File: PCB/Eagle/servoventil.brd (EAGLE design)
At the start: 160 x 100 mm, 0 parts

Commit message: Rozdělané schéma
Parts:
- added C1, C2: 100n 1206, rcl:C1206
- added D1: LOW BAT 1206, SparkFun-LED:LED-1206
- added D2: STTH4R02S DO214AB, diode:DO214AA
- added DIP: DIP-4X_DIP, #PaJa_prepinace:DIP-4X
- added F1: 3,5A 1206, adafruit:R1206
- added IO1: ATTINY1634 SO20W, bt_avr:SOIC20
- added IO2: MCP1825 SOT223, bt_regulator:SOT-223-3
- added IO3: DS3231MZ+, SamacSys_Parts:SOIC127P600X175-8N
- added J1: ICSP 2x5, SparkFun-Connectors:2X5-SHROUDED_LOCK
- added J2: SERIAL, #PaJa_konektory:S1G5_JUM
- added K1: ARK500/2, #PaJa_konektory:ARK500/2
- added R1, R8: 10k 1206, rcl:R1206
- added R10, R9: 4k7 1206, rcl:R1206
- added R2: 10k 1203, rcl:R1206
- added R3: 1k 1206, rcl:R1206
- added R4: 47k 1206, rcl:R1206
- added R5: 2k7 1206, rcl:R1206
- added R6: 3k3 1206, rcl:R1206
- added R7: 100R 1206, rcl:R1206
- added S1: 6x6mm SMD, SparkFun-Switches:TACTILE_SWITCH_SMD_6.2MM_TALL
- added T1: DMP2100U SOT23, bt_transistor:SOT-23
- added T2: IRF7416PBF SO8, SamacSys_Parts:SOIC127P600X175-8N
- added T3: FDV303N SOT23, bt_transistor:SOT-23
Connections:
- new net 3,3V_VCC: C2.1, IO2.3, IO3.2, R10.1, R9.1
- new net 6V: C1.1, IO2.1, R5.2, T1.3
- new net GND: C1.2, C2.2, D1.C, D2.A, DIP.1, DIP.2, DIP.3, DIP.4, IO1.10, IO3.5, J1.10, J1.4, J1.6, J1.8, J2.1, K1.1, R4.1, R6.1, S1.A2, T3.2
- new net HEATSINK: IO2.2, IO2.4
- new net LED_LOWBAT_PIN: R7.1
- new net LOW_BAT_PIN: R5.1, R6.2
- new net N$1: F1.2, K1.2
- new net N$10: IO3.3
- new net N$12: D1.A, R7.2
- new net N$2: D2.C, F1.1, R1.2, R2.2, T1.2, T2.1, T2.2, T2.3
- new net N$3: R3.2, R4.2, T3.1
- new net N$5: J1.7
- new net N$6: J1.9
- new net N$7: J1.1
- new net PWR_ON_PIN: R3.1
- new net PWR_RTC_ON: R1.1, S1.B2, T1.1, T3.3
- new net PWR_SERVO_ON_PIN: R2.1, T2.4
- new net PWR_SERVO_OUT: T2.5, T2.6, T2.7, T2.8
- new net RESET: IO1.14, J1.5, J2.5, R8.2
- new net RX_PIN: J2.4
- new net SCL_PIN: IO3.8, R9.2
- new net SDA_PIN: IO3.7, R10.2
- new net SW1_PIN: DIP.8
- new net SW2_PIN: DIP.7
- new net SW3_PIN: DIP.6
- new net SW4_PIN: DIP.5
- new net TX_PIN: J2.3
- new net VCC: IO1.11, J1.2, J2.2, R8.1

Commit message: Schema před kontrolou
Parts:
- removed IO3: DS3231MZ+, SamacSys_Parts:SOIC127P600X175-8N
- removed S1: 6x6mm SMD, SparkFun-Switches:TACTILE_SWITCH_SMD_6.2MM_TALL
- added BT1: CR2032, SparkFun-Batteries:BATTCOM_20MM_PTH
- added IO3A: DS3231MZ+ SO8, SamacSys_Parts:SOIC127P600X175-8N
- added IO3B: DS3231SN SO16W, adafruit:SO16W
- added SW1: SPST_TACT-EVQQ2, adafruit:EVQ-Q2
- moved R10 251.6 mm to (66.0, 78.7), turned to 270 degrees
- moved R9 244.2 mm to (62.2, 78.7), turned to 270 degrees
- moved C1 205.0 mm to (133.3, 86.4)
- moved C2 205.0 mm to (133.3, 81.3)
- moved R1 205.0 mm to (133.3, 76.2)
- moved R2 205.0 mm to (133.3, 71.1)
- moved R3 205.0 mm to (128.3, 38.1)
- moved R4 205.0 mm to (128.3, 31.8)
- moved R5 205.0 mm to (128.3, 25.4)
- moved R6 205.0 mm to (128.3, 19.1)
- moved R7 205.0 mm to (115.6, 12.7)
- moved R8 205.0 mm to (115.6, 6.35)
- moved K1 202.6 mm to (144.8, 31.8)
- moved DIP 202.5 mm to (80.0, 57.1)
- moved T2 195.2 mm to (114.3, 50.8)
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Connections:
- removed net N$10: IO3.3
- removed net N$5: J1.7
- removed net N$6: J1.9
- removed net N$7: J1.1
- removed net SCL_PIN: IO3.8, R9.2
- removed net SDA_PIN: IO3.7, R10.2
- new net 3V: BT1.1, IO3A.6, IO3B.14
- new net MISO: IO1.19, J1.9
- new net MOSI_SDA_PIN: IO1.20, IO3A.7, IO3B.15, J1.1, R10.2
- new net SCK_SCL_PIN: IO1.16, IO3A.8, IO3B.16, J1.7, R9.2
- new net SERVO_PIN: IO1.4
- net 3,3V_VCC: now also IO3A.2, IO3B.2; no longer IO3.2
- net GND: now also BT1.2, IO3A.5, IO3B.10, IO3B.11, IO3B.12, IO3B.13, IO3B.5, IO3B.6, IO3B.7, IO3B.8, IO3B.9, SW1.A, SW1.A'; no longer IO3.5, S1.A2
- net LED_LOWBAT_PIN: now also IO1.7
- net LOW_BAT_PIN: now also IO1.6
- net PWR_ON_PIN: now also IO1.5
- net PWR_RTC_ON: now also IO3A.3, IO3B.3, SW1.B, SW1.B'; no longer S1.B2
- net PWR_SERVO_ON_PIN: now also IO1.3
- net RX_PIN: now also IO1.2
- net SW1_PIN: now also IO1.8
- net SW2_PIN: now also IO1.9
- net SW3_PIN: now also IO1.12
- net SW4_PIN: now also IO1.13
- net TX_PIN: now also IO1.1

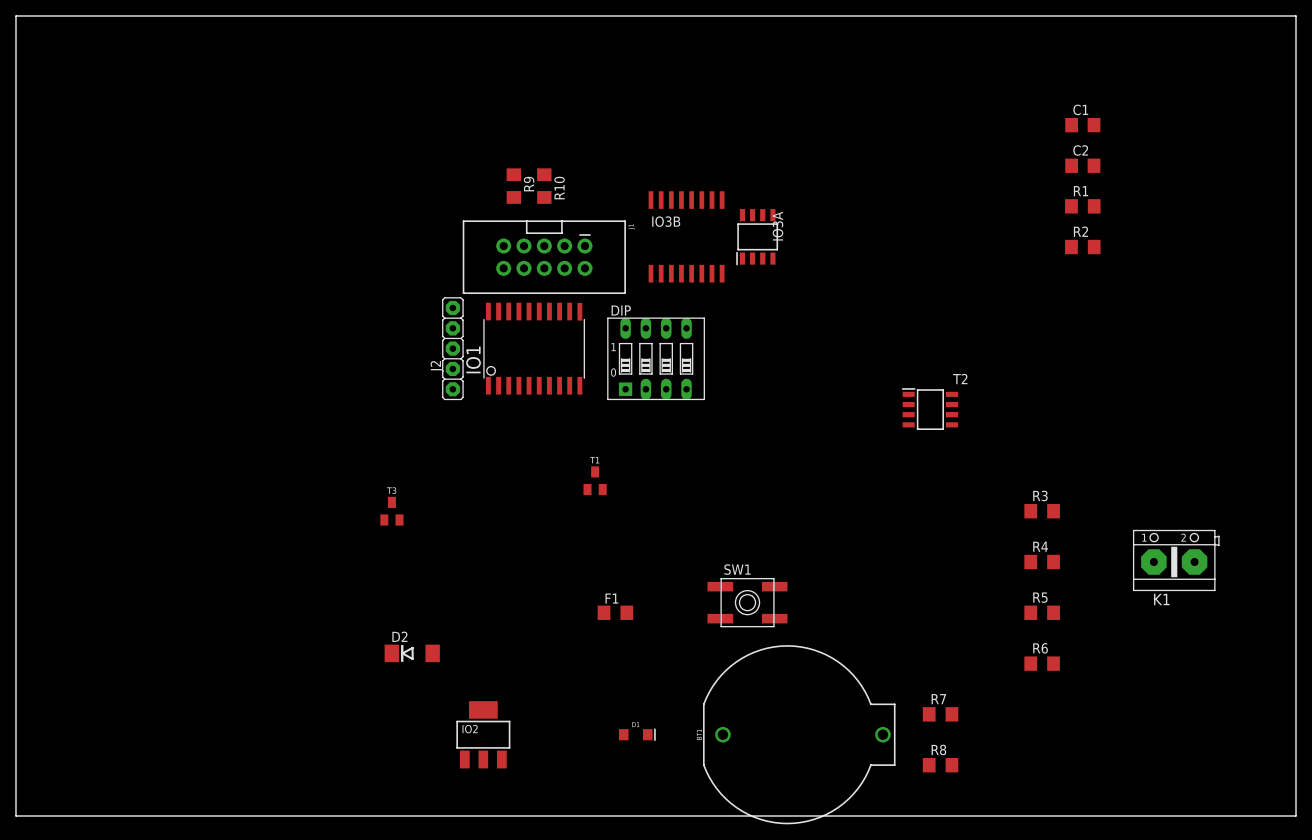
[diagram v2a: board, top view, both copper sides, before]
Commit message: Deska spojů, schéma
vše před kontrolou (až dorazí součástky)
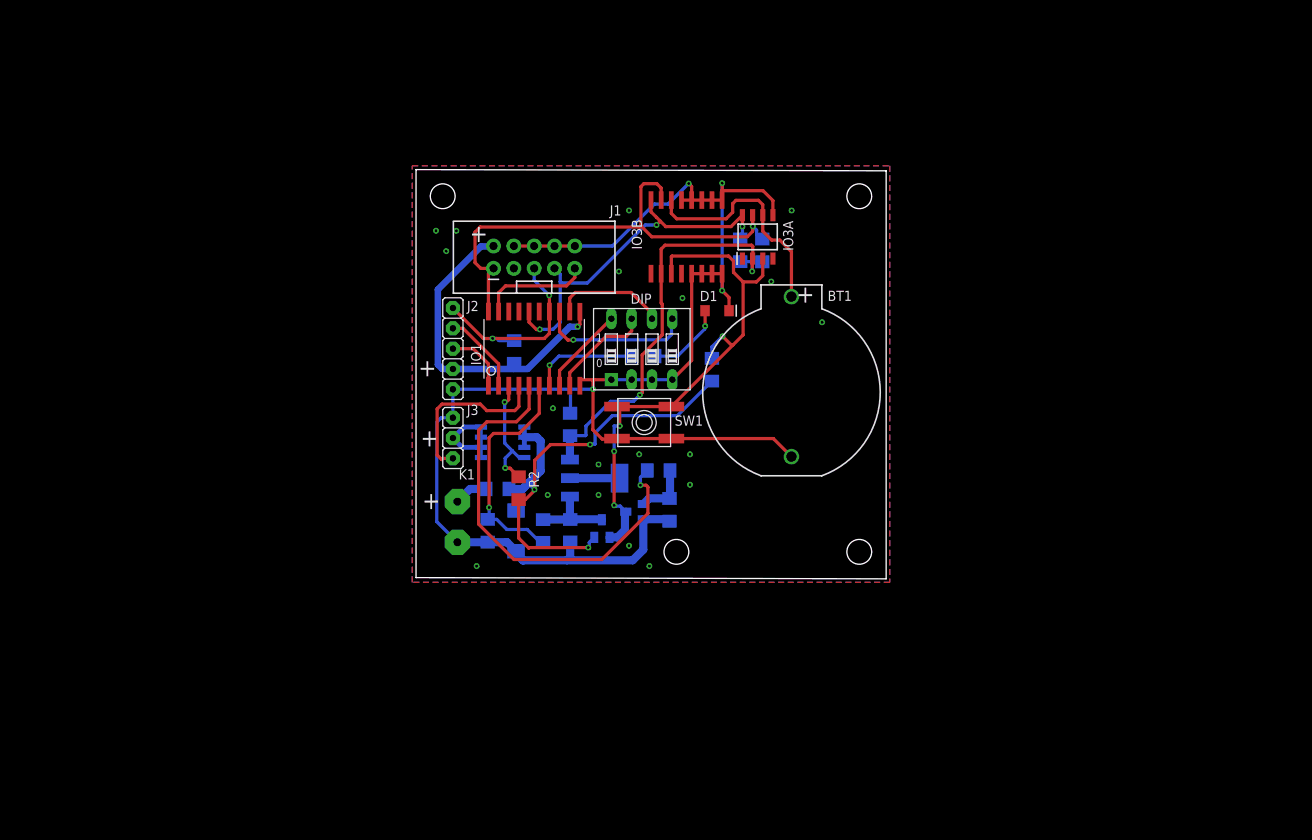
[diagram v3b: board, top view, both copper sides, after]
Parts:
- added J3: SERVO, #PaJa_konektory:S1G3_JUM
- moved K1 89.7 mm to (55.2, 36.8), flipped to the bottom, turned to 90 degrees
- moved C1 81.7 mm to (69.3, 35.7), flipped to the bottom, turned to 270 degrees
- moved R2 76.7 mm to (62.8, 41.0), turned to 270 degrees
- moved R8 74.2 mm to (62.3, 58.0), flipped to the bottom, turned to 90 degrees
- moved C2 71.8 mm to (69.3, 48.9), flipped to the bottom, turned to 90 degrees
- moved R6 71.3 mm to (59.0, 35.7), flipped to the bottom, turned to 90 degrees
- moved R5 63.2 mm to (65.9, 35.6), flipped to the bottom, turned to 90 degrees
- moved R7 58.2 mm to (78.5, 57.5), flipped to the bottom, turned to 180 degrees
- moved D1 54.0 mm to (87.6, 63.2)
- moved T2 53.6 mm to (60.8, 46.7), flipped to the bottom
- moved R1 50.7 mm to (87.0, 55.8), flipped to the bottom, turned to 270 degrees
- moved R3 48.2 mm to (80.3, 43.2), flipped to the bottom, turned to 180 degrees
- moved R4 47.0 mm to (81.7, 38.3), flipped to the bottom, turned to 90 degrees
- moved BT1 42.9 mm to (96.9, 53.1), turned to 90 degrees
- moved IO2 35.0 mm to (72.3, 42.2), flipped to the bottom, turned to 90 degrees
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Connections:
- net GND: now also J3.3
- net PWR_SERVO_OUT: now also J3.2
- net SERVO_PIN: now also J3.1
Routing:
- net GND: track 0.00 -> 201.7 mm, vias 0 -> 23
- net PWR_RTC_ON: track 0.00 -> 68.8 mm, vias 0 -> 4
- net N$2: track 0.00 -> 67.0 mm, vias 0 -> 3
- net MOSI_SDA_PIN: track 0.00 -> 62.9 mm, vias 0 -> 1
- net PWR_ON_PIN: track 0.00 -> 54.0 mm, vias 0 -> 1
- net 3,3V_VCC: track 0.00 -> 52.8 mm, vias 0 -> 2
- net SCK_SCL_PIN: track 0.00 -> 46.1 mm, vias 0 -> 3
- net VCC: track 0.00 -> 41.2 mm, vias 0 -> 1
- net LOW_BAT_PIN: track 0.00 -> 29.4 mm, vias 0 -> 1
- net 3V: track 0.00 -> 28.8 mm
- net RESET: track 0.00 -> 25.6 mm, vias 0 -> 2
- net SERVO_PIN: track 0.00 -> 21.7 mm
- net SW4_PIN: track 0.00 -> 19.2 mm, vias 0 -> 1
- net PWR_SERVO_ON_PIN: track 0.00 -> 15.4 mm, vias 0 -> 2
- net SW3_PIN: track 0.00 -> 14.1 mm
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- added copper zone on layer 1, net GND
- added copper zone on layer 16, net GND
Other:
- board size 160 x 100 mm -> 58.8 x 51.2 mm
- board text added: "+"
- board text added: "G"
- board text added: "ICSP"
- board text added: "R"
- board text added: "RST"
- board text added: "S"
- board text added: "SERVOVENTIL 1.0-1401209 PIHRT.COM"
- board text added: "T"

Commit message: Schéma a deska před kontrolou
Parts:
- added J4: I2C, #PaJa_konektory:S1G4_JUM
- added R11: 1k 1206, rcl:R1206
- added R12: 47k 1206, rcl:R1206
- added T4: FDV303N SOT23, bt_transistor:SOT-23
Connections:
- removed net 3,3V_VCC: C2.1, IO2.3, IO3A.2, IO3B.2, R10.1, R9.1
- new net N$4: R2.1, T2.4, T4.3
- new net N$5: R11.2, R12.2, T4.1
- net GND: now also J4.1, R12.1, T4.2
- net MOSI_SDA_PIN: now also J4.3
- net PWR_SERVO_ON_PIN: now also R11.1; no longer R2.1, T2.4
- net SCK_SCL_PIN: now also J4.4
- net VCC: now also C2.1, IO2.3, IO3A.2, IO3B.2, J4.2, R10.1, R9.1
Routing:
- net VCC: track 41.2 -> 158.0 mm, vias 1 -> 4
- net GND: track 201.7 -> 289.0 mm, vias 23 -> 24
- net 3,3V_VCC: track 52.8 -> 0.00 mm, vias 2 -> 0
- net SCK_SCL_PIN: track 46.1 -> 57.1 mm, vias 3 -> 5
- net N$4: track 0.00 -> 10.8 mm, vias 0 -> 1
- net N$5: track 0.00 -> 6.44 mm
- net MOSI_SDA_PIN: track 62.9 -> 66.1 mm
- net PWR_SERVO_ON_PIN: track 15.4 -> 18.5 mm
- net N$2: track 67.0 -> 68.1 mm
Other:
- outline, holes or cut-outs redrawn
- board text added: "A"
- board text added: "I2C"
- board text added: "SCL"
- board text added: "SERVOVENTIL 1.0-1501209 PIHRT.COM"
- board text removed: "SERVOVENTIL 1.0-1401209 PIHRT.COM"

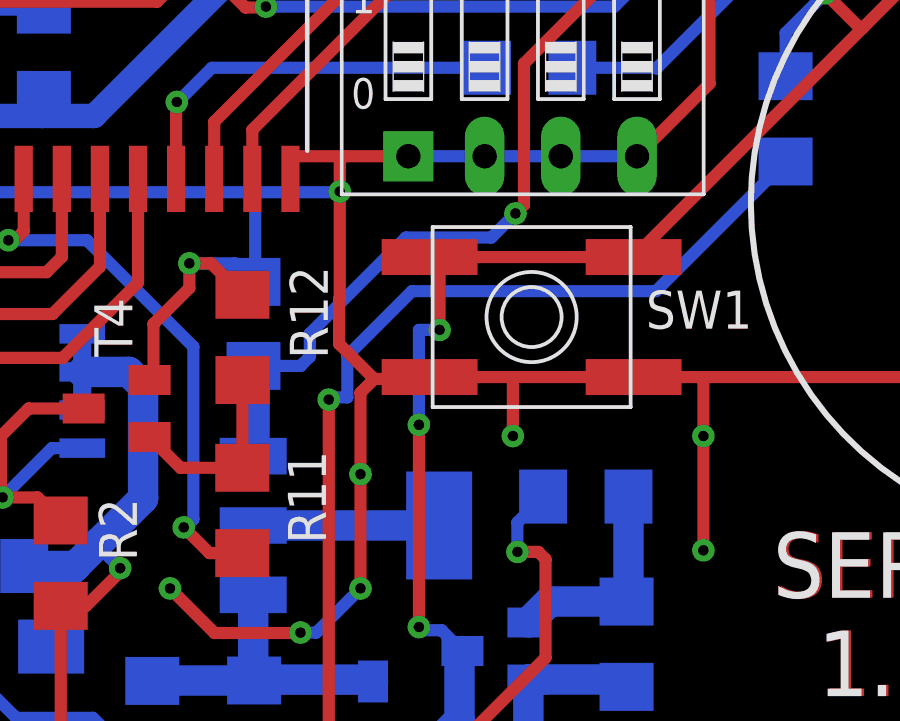
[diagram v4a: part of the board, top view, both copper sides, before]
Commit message: oprava chyby na desce
chyběla zem pod 3,3V stabilizátorem (heatsink + gnd se nespojilo)
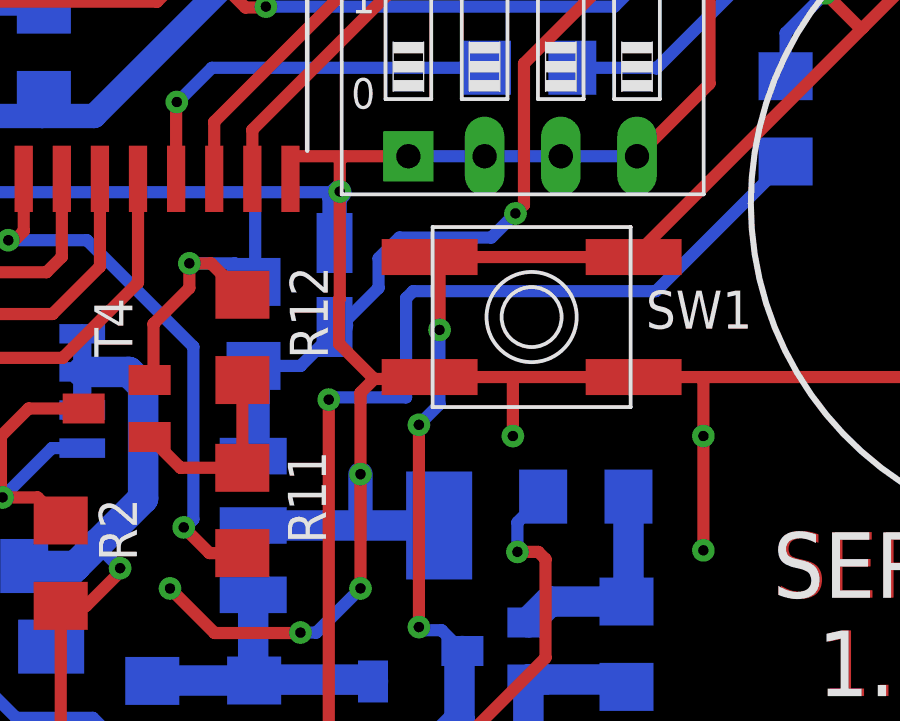
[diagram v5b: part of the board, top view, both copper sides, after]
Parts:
- added C3: 22uF 6,3V tant 1206, rcl:CT3216
- C1: value 100n 1206 -> 470n 1206
- IO2: value MCP1825 SOT223 -> TS2940CW-3.3 SOT223
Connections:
- removed net HEATSINK: IO2.2, IO2.4
- net GND: now also C3.-, IO2.2, IO2.4
- net VCC: now also C3.+
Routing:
- net GND: track 289.0 -> 298.6 mm
- net HEATSINK: track 6.20 -> 0.00 mm
- net N$2: track 68.1 -> 69.2 mm
